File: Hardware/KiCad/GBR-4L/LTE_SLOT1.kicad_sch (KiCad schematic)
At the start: 0 parts

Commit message: Add modem and SIM schematics
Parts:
- added C101, C102, C103, C104: 100nF, Capacitor_SMD:C_0603_1608Metric, symbol Device:C
- added C105, C106: 100uF 6.3V low-ESR, Capacitor_SMD:C_1210_3225Metric, symbol Device:C
- added J101: EM7565 M.2 Key B socket, symbol Connector:Bus_M.2_Socket_B
- added J102: MODEM_CONTROL, Connector_PinHeader_2.54mm:PinHeader_1x08_P2.54mm_Vertical, symbol Connector_Generic:Conn_01x08
- added R101: 10k, Resistor_SMD:R_0603_1608Metric, symbol Device:R
- added R102, R103: 100R, Resistor_SMD:R_0603_1608Metric, symbol Device:R
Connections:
- new net +3V3_M1: C101.1, C102.1, C103.1, C104.1, C105.1, C106.1, J101.2 (3.3V), J101.4 (3.3V), J101.70 (3.3V), J101.72 (3.3V), J101.74 (3.3V), J102.1 (Pin_1), R101.1
- new net GND: C101.2, C102.2, C103.2, C104.2, C105.2, C106.2, J101.11 (GND), J101.27 (GND), J101.3 (GND), J101.33 (GND), J101.39 (GND), J101.45 (GND), J101.5 (GND), J101.51 (GND), J101.57 (GND), J101.71 (GND), J101.73 (GND), J102.2 (Pin_2)
- new net M1_FULL_CARD_POWER_OFF#: J101.6 (~{FULL_CARD_POWER_OFF}), J102.4 (Pin_4), R101.2
- new net M1_PWR_EN: J102.3 (Pin_3)
- new net M1_RESET#: J101.67 (~{RESET}), R102.2
- new net M1_RESET_CTRL#: J102.5 (Pin_5), R102.1
- new net M1_SIM_DETECT: J101.66 (SIM_DETECT), J102.8 (Pin_8)
- new net M1_UIM_CLK: J101.32 (UIM-CLK)
- new net M1_UIM_DATA: J101.34 (UIM-DATA)
- new net M1_UIM_PWR: J101.36 (UIM-PWR)
- new net M1_UIM_RESET: J101.30 (UIM-RESET)
- new net M1_WWAN_LED#: J101.10 (GPIO_9/DAS/~{DSS}/~{LED1}), J102.7 (Pin_7)
- new net M1_W_DISABLE#: J101.8 (~{W_DISABLE1}), R103.2
- new net M1_W_DISABLE_CTRL#: J102.6 (Pin_6), R103.1
- new net USB_M1_D+: J101.7 (USB_D+)
- new net USB_M1_D-: J101.9 (USB_D-)
- no-connect marks 0 -> 40
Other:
- note added: "Do not drive module I/O until at least 100 ms after the start of power-up."
- note added: "EM7565 MODEM SLOT 1 — M.2 KEY B 3042"
- note added: "M.2 socket footprint intentionally remains unassigned until the connector height is frozen."
- note added: "Route USB as 90-ohm differential; keep the pair on continuous ground and away from buck switch nodes."
- note added: "USB 2.0 only. PCIe, USB 3.0, secondary SIM, antenna-control and reserved pins are NC."
- title: (none) -> GBR-4L EM7565 slot 1

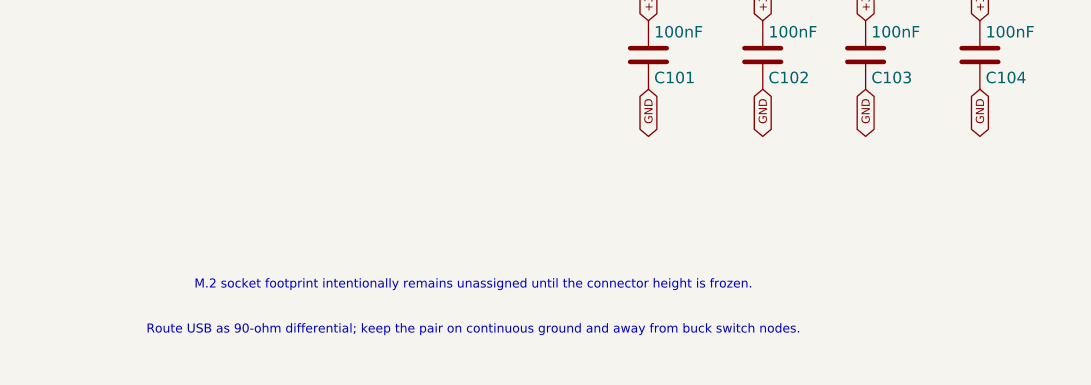
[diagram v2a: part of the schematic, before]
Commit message: Add connector footprints and initial PCB packing
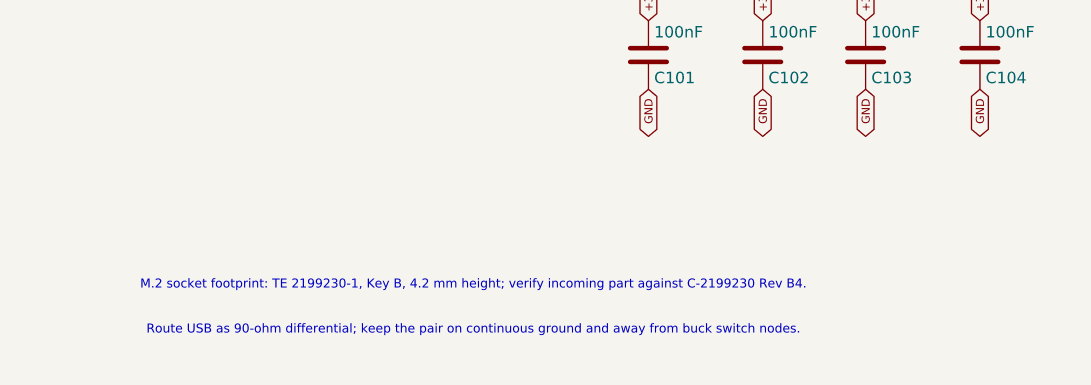
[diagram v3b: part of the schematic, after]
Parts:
- J101: footprint (none) -> GBR-4L:TE_2199230-1_M2_Key-B
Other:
- note added: "M.2 socket footprint: TE 2199230-1, Key B, 4.2 mm height; verify incoming part against C-2199230 Rev B4."
- note removed: "M.2 socket footprint intentionally remains unassigned until the connector height is frozen."
